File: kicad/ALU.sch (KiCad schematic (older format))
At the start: 41 parts

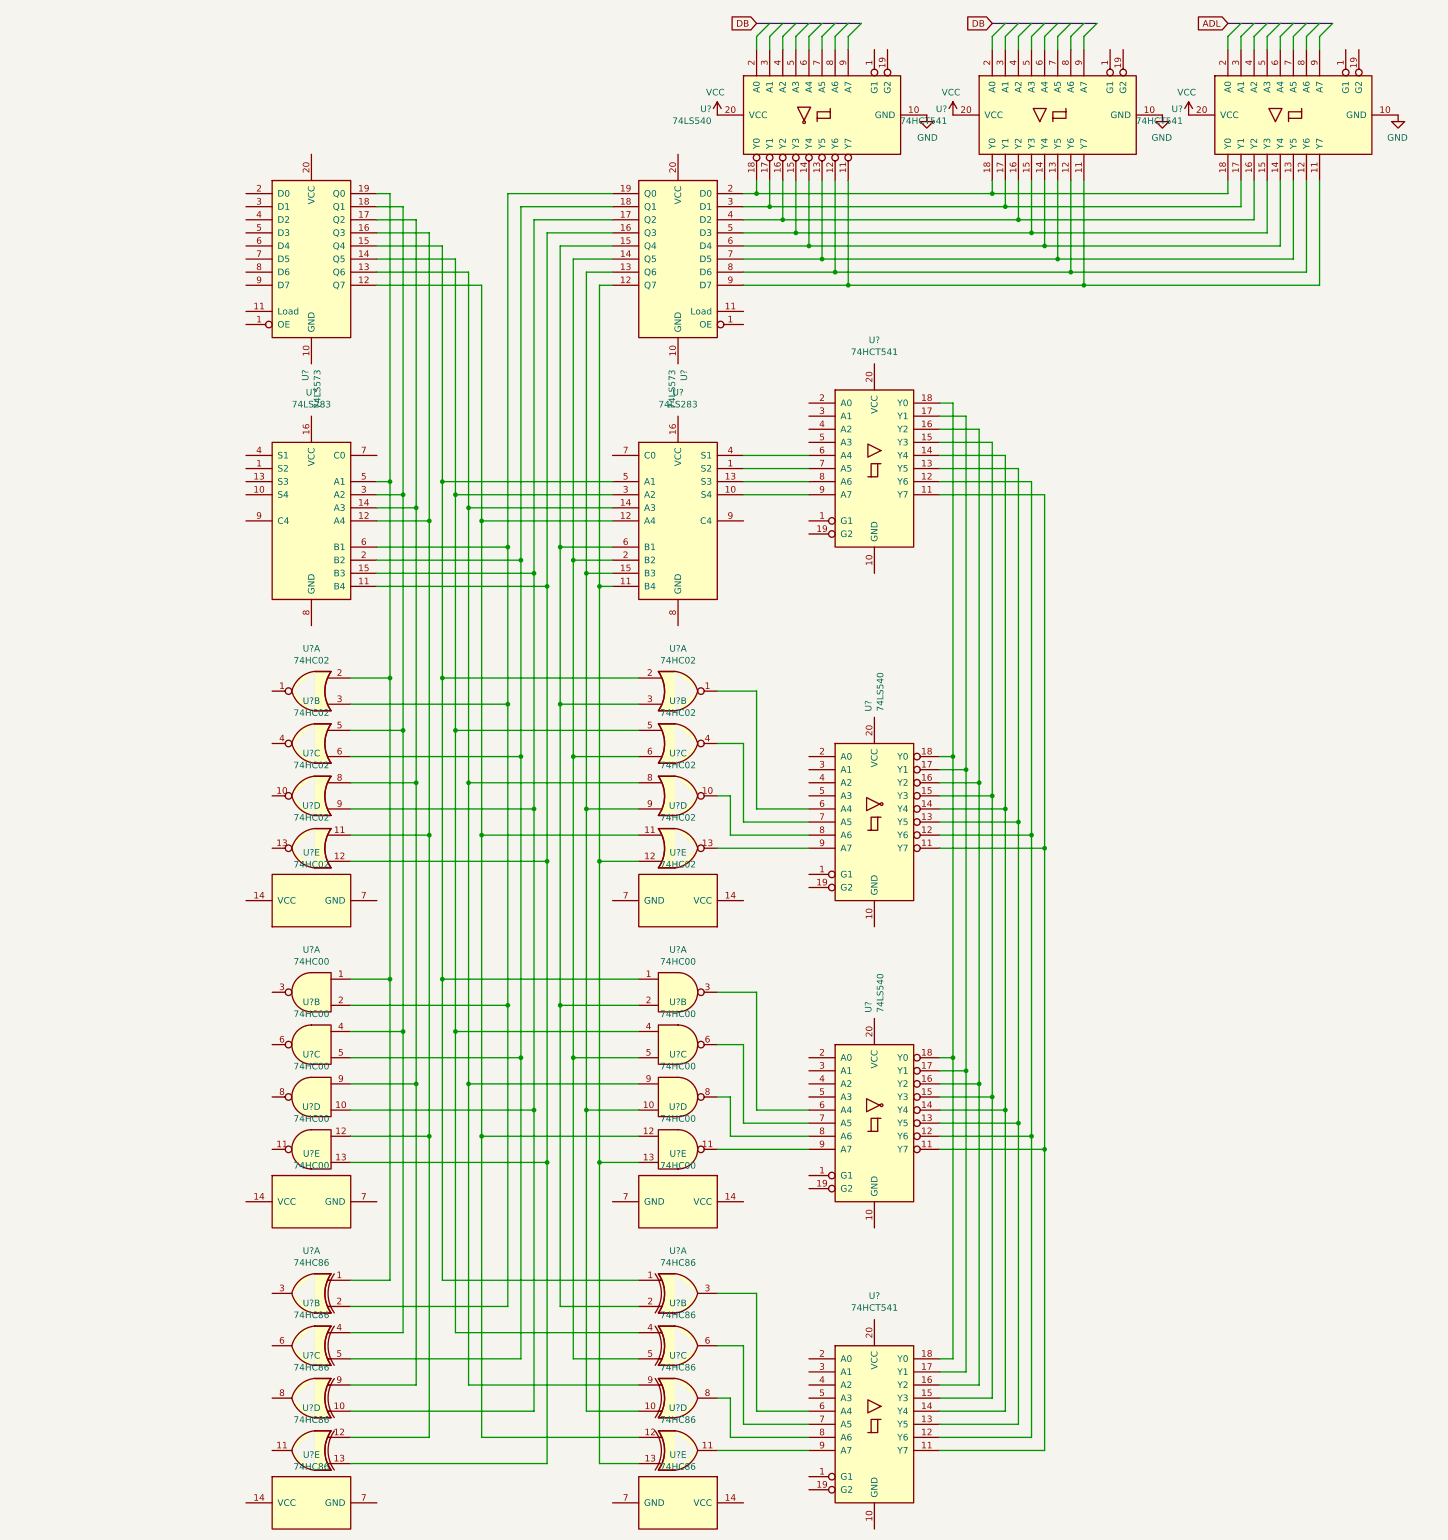
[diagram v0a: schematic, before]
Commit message: add ALU schematic
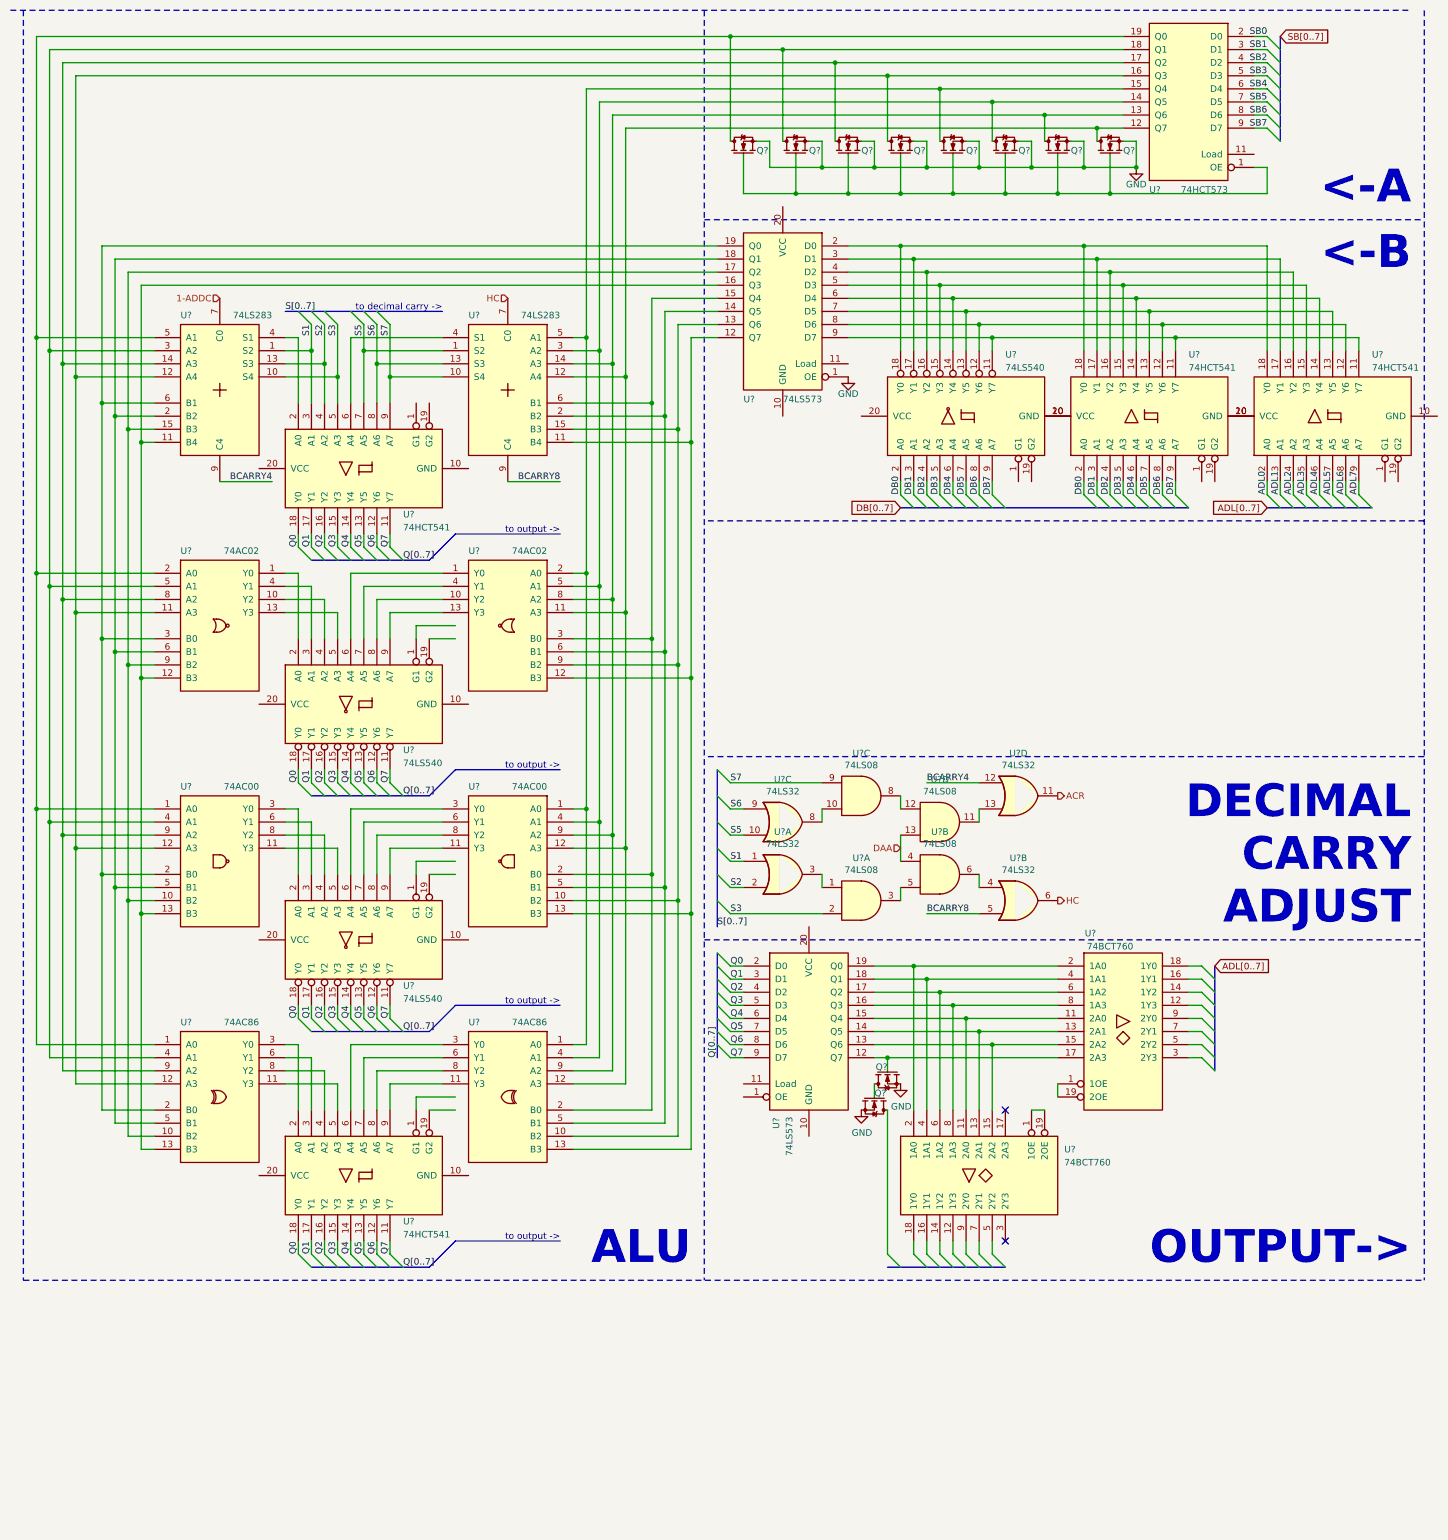
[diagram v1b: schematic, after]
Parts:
- removed U? (x2): 74LS573, symbol 74xx:74LS573
- removed U? (x4): 74HCT541, symbol 74xx:74HCT541
- removed U? (x3): 74LS540, symbol 74xx:74LS540
- removed U? (x2): 74LS283, symbol 74xx:74LS283
- removed U? (x10): 74HC02, symbol 74xx:74HC02
- removed U? (x10): 74HC00, symbol 74xx:74HC00
- removed U? (x10): 74HC86, symbol 74xx:74HC86
- added Q? (x10): VN2106, Package_TO_SOT_THT:TO-92_Inline, symbol 6502:VN2106
- added U? (x2): 74LS573, symbol 74xx:74LS573
- added U? (x3): 74LS540, symbol 74xx:74LS540
- added U?: 74HCT573, symbol 6502:74HCT573
- added U? (x4): 74HCT541, symbol 74xx:74HCT541
- added U? (x2): 74LS283, symbol 6502:74HC283
- added U? (x2): 74BCT760, symbol 6502:74BCT760
- added U? (x2): 74AC02, symbol 6502:74AC02
- added U? (x2): 74AC00, symbol 6502:74AC00
- added U? (x2): 74AC86, symbol 6502:74AC86
- added U? (x4): 74LS32, symbol 74xx:74LS32
- added U? (x4): 74LS08, symbol 74xx:74LS08
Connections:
- net GND: now also Q?.3 (S), Q?.3 (S), Q?.3 (S), Q?.3 (S), Q?.3 (S), Q?.3 (S), Q?.3 (S), Q?.3 (S), Q?.3 (S), Q?.3 (S), U?.1 (OE), U?.10 (GND), U?.10 (GND), U?.10 (GND), U?.7 (GND), U?.7 (GND), U?.7 (GND), U?.7 (GND), U?.7 (GND), U?.7 (GND), U?.8 (GND), U?.8 (GND)
- net VCC: now also U?.14 (VCC), U?.14 (VCC), U?.14 (VCC), U?.14 (VCC), U?.14 (VCC), U?.14 (VCC), U?.16 (VCC), U?.16 (VCC), U?.20 (VCC), U?.20 (VCC), U?.20 (VCC)
- new net: Q?.1 (D), Q?.2 (G)
- new net: Q?.2 (G), U?.12 (Q7), U?.17 (2A3)
- new net: Q?.1 (D), U?.1 (A0), U?.1 (A0), U?.19 (Q0), U?.2 (A0), U?.5 (A1)
- new net: Q?.2 (G), Q?.2 (G), Q?.2 (G), Q?.2 (G), Q?.2 (G), Q?.2 (G), Q?.2 (G), Q?.2 (G), U?.1 (OE)
- new net: Q?.1 (D), U?.18 (Q1), U?.3 (A2), U?.4 (A1), U?.4 (A1), U?.5 (A1)
- new net: Q?.1 (D), U?.14 (A3), U?.17 (Q2), U?.8 (A2), U?.9 (A2), U?.9 (A2)
- new net: Q?.1 (D), U?.11 (A3), U?.12 (A3), U?.12 (A3), U?.12 (A4), U?.16 (Q3)
- new net: Q?.1 (D), U?.1 (A0), U?.1 (A0), U?.15 (Q4), U?.2 (A0), U?.5 (A1)
- new net: Q?.1 (D), U?.14 (Q5), U?.3 (A2), U?.4 (A1), U?.4 (A1), U?.5 (A1)
- new net: Q?.1 (D), U?.13 (Q6), U?.14 (A3), U?.8 (A2), U?.9 (A2), U?.9 (A2)
- new net: Q?.1 (D), U?.11 (A3), U?.12 (A3), U?.12 (A3), U?.12 (A4), U?.12 (Q7)
- new net: U?.11 (B4), U?.12 (B3), U?.12 (Q7), U?.13 (B3), U?.13 (B3)
- new net: U?.10 (B2), U?.10 (B2), U?.13 (Q6), U?.15 (B3), U?.9 (B2)
- new net: U?.14 (Q5), U?.2 (B2), U?.5 (B1), U?.5 (B1), U?.6 (B1)
- new net: U?.15 (Q4), U?.2 (B0), U?.2 (B0), U?.3 (B0), U?.6 (B1)
- new net: U?.11 (B4), U?.12 (B3), U?.13 (B3), U?.13 (B3), U?.16 (Q3)
- new net: U?.10 (B2), U?.10 (B2), U?.15 (B3), U?.17 (Q2), U?.9 (B2)
- new net: U?.18 (Q1), U?.2 (B2), U?.5 (B1), U?.5 (B1), U?.6 (B1)
- new net: U?.19 (Q0), U?.2 (B0), U?.2 (B0), U?.3 (B0), U?.6 (B1)
- new net: U?.18 (Y0), U?.18 (Y0), U?.18 (Y0), U?.2 (D0)
- new net: U?.17 (Y1), U?.17 (Y1), U?.17 (Y1), U?.3 (D1)
- new net: U?.16 (Y2), U?.16 (Y2), U?.16 (Y2), U?.4 (D2)
- new net: U?.15 (Y3), U?.15 (Y3), U?.15 (Y3), U?.5 (D3)
- new net: U?.14 (Y4), U?.14 (Y4), U?.14 (Y4), U?.6 (D4)
- new net: U?.13 (Y5), U?.13 (Y5), U?.13 (Y5), U?.7 (D5)
- new net: U?.12 (Y6), U?.12 (Y6), U?.12 (Y6), U?.8 (D6)
- new net: U?.11 (Y7), U?.11 (Y7), U?.11 (Y7), U?.9 (D7)
- new net: U?.4 (S1), U?.6 (A4)
- new net: U?.2 (A0), U?.4 (S1)
- new net: U?.1 (Y0), U?.2 (A0)
- new net: U?.3 (A1), U?.4 (Y1)
- new net: U?.10 (Y2), U?.4 (A2)
- new net: U?.13 (Y3), U?.5 (A3)
- new net: U?.1 (Y0), U?.6 (A4)
- new net: U?.4 (Y1), U?.7 (A5)
- new net: U?.10 (Y2), U?.8 (A6)
- new net: U?.13 (Y3), U?.9 (A7)
- new net: U?.13 (Q6), U?.15 (2A2), U?.15 (2A2)
- new net: U?.13 (2A1), U?.13 (2A1), U?.14 (Q5)
- new net: U?.11 (2A0), U?.11 (2A0), U?.15 (Q4)
- new net: U?.16 (Q3), U?.8 (1A3), U?.8 (1A3)
- new net: U?.17 (Q2), U?.6 (1A2), U?.6 (1A2)
- new net: U?.18 (Q1), U?.4 (1A1), U?.4 (1A1)
- new net: U?.19 (Q0), U?.2 (1A0), U?.2 (1A0)
- new net: U?.1 (1OE), U?.19 (2OE) (x2)
- new net: U?.2 (A0), U?.3 (Y0) (x2)
- new net: U?.3 (A1), U?.6 (Y1) (x2)
- new net: U?.4 (A2), U?.8 (Y2) (x2)
- new net: U?.11 (Y3), U?.5 (A3) (x2)
- new net: U?.3 (Y0), U?.6 (A4) (x2)
- new net: U?.6 (Y1), U?.7 (A5) (x2)
- new net: U?.8 (A6), U?.8 (Y2) (x2)
- new net: U?.11 (Y3), U?.9 (A7) (x2)
- new net: U?.1, U?.3
- new net: U?.4, U?.6
- new net: U?.10, U?.8
- new net: U?.11, U?.13
- new net: U?.3, U?.5
- new net: U?.12, U?.8
- new net 1-ADDC: U?.7 (C0)
- new net ACR: U?.11
- new net ADL0: U?.2 (A0)
- new net ADL1: U?.3 (A1)
- new net ADL2: U?.4 (A2)
- new net ADL3: U?.5 (A3)
- new net ADL4: U?.6 (A4)
- new net ADL5: U?.7 (A5)
- new net ADL6: U?.8 (A6)
- new net ADL7: U?.9 (A7)
- new net BCARRY4: U?.12, U?.9 (C4)
- new net BCARRY8: U?.5, U?.9 (C4)
- new net DAA: U?.13, U?.4
- new net DB0: U?.2 (A0), U?.2 (A0)
- new net DB1: U?.3 (A1), U?.3 (A1)
- new net DB2: U?.4 (A2), U?.4 (A2)
- new net DB3: U?.5 (A3), U?.5 (A3)
- new net DB4: U?.6 (A4), U?.6 (A4)
- new net DB5: U?.7 (A5), U?.7 (A5)
- new net DB6: U?.8 (A6), U?.8 (A6)
- new net DB7: U?.9 (A7), U?.9 (A7)
- new net HC: U?.6, U?.7 (C0)
- new net Q0: U?.18 (Y0), U?.18 (Y0), U?.18 (Y0), U?.18 (Y0), U?.2 (D0)
- new net Q1: U?.17 (Y1), U?.17 (Y1), U?.17 (Y1), U?.17 (Y1), U?.3 (D1)
- new net Q2: U?.16 (Y2), U?.16 (Y2), U?.16 (Y2), U?.16 (Y2), U?.4 (D2)
- new net Q3: U?.15 (Y3), U?.15 (Y3), U?.15 (Y3), U?.15 (Y3), U?.5 (D3)
- new net Q4: U?.14 (Y4), U?.14 (Y4), U?.14 (Y4), U?.14 (Y4), U?.6 (D4)
- new net Q5: U?.13 (Y5), U?.13 (Y5), U?.13 (Y5), U?.13 (Y5), U?.7 (D5)
- new net Q6: U?.12 (Y6), U?.12 (Y6), U?.12 (Y6), U?.12 (Y6), U?.8 (D6)
- new net Q7: U?.11 (Y7), U?.11 (Y7), U?.11 (Y7), U?.11 (Y7), U?.9 (D7)
- new net S1: U?.1, U?.1 (S2), U?.3 (A1)
- new net S2: U?.13 (S3), U?.2, U?.4 (A2)
- new net S3: U?.10 (S4), U?.2, U?.5 (A3)
- new net S5: U?.1 (S2), U?.10, U?.7 (A5)
- new net S6: U?.13 (S3), U?.8 (A6), U?.9
- new net S7: U?.10 (S4), U?.9, U?.9 (A7)
- new net SB0: U?.2 (D0)
- new net SB1: U?.3 (D1)
- new net SB2: U?.4 (D2)
- new net SB3: U?.5 (D3)
- new net SB4: U?.6 (D4)
- new net SB5: U?.7 (D5)
- new net SB6: U?.8 (D6)
- new net SB7: U?.9 (D7)
- no-connect marks 0 -> 2
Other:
- note added: "<-A"
- note added: "<-B"
- note added: "ALU"
- note added: "DECIMAL\nCARRY\nADJUST"
- note added: "OUTPUT->"
- note added: "to decimal carry ->"
- note added: "to output ->"

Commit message: use custom components
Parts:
- U? (x2): value 74LS573 -> 74HCT573; symbol 74xx:74LS573 -> 6502:74HCT573
- U? (x3): value 74LS540 -> 74HC540; symbol 74xx:74LS540 -> 6502:74HC540
- U? (x4): value 74HCT541 -> 74HC541; symbol 74xx:74HCT541 -> 6502:74HC541
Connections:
- net GND: now also U?.10 (GND), U?.10 (GND), U?.10 (GND), U?.10 (GND), U?.10 (GND), U?.10 (GND), U?.10 (GND), U?.10 (GND), U?.10 (GND)
- net VCC: now also U?.20 (VCC), U?.20 (VCC), U?.20 (VCC), U?.20 (VCC), U?.20 (VCC), U?.20 (VCC), U?.20 (VCC), U?.20 (VCC), U?.20 (VCC)
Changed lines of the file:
@@
 $Descr A3 11693 16535 portrait
 encoding utf-8
-Sheet 3 3
+Sheet 2 2
 Title ""
 Date ""
@@
 	1400 3800 1500 3800
 $Comp
-L 74xx:74HCT541 U?
+L 6502:74HC541 U?
 U 1 1 63074D6C
 P 3100 4000
@@
 AR Path="/628D8D48/63074D6C" Ref="U?"  Part="1"
 F 0 "U?" V 3450 3700 50  0000 R CNN
-F 1 "74HCT541" V 3550 3700 50  0000 R CNN
+F 1 "74HC541" V 3550 3700 50  0000 R CNN
 F 2 "" H 3100 4000 50  0001 C CNN
-F 3 "http://www.ti.com/lit/gpn/sn74HCT541" H 3100 4000 50  0001 C CNN
+F 3 "http://www.ti.com/lit/gpn/sn74LS540" H 3100 4000 50  0001 C CNN
 	1    3100 4000
 	0    -1   1    0
@@
 Q7
 $Comp
-L 74xx:74LS540 U?
+L 6502:74HC540 U?
 U 1 1 63D46498
 P 3100 5800
@@
 AR Path="/628D8D48/63D46498" Ref="U?"  Part="1"
 F 0 "U?" V 3450 5500 50  0000 R CNN
-F 1 "74LS540" V 3550 5500 50  0000 R CNN
+F 1 "74HC540" V 3550 5500 50  0000 R CNN
 F 2 "" H 3100 5800 50  0001 C CNN
 F 3 "http://www.ti.com/lit/gpn/sn74LS540" H 3100 5800 50  0001 C CNN
@@
 $EndComp
 $Comp
-L 74xx:74LS573 U?
+L 6502:74HCT573 U?
 U 1 1 63DA36B1
 P 6500 8300
@@
 AR Path="/628D8D48/63DA36B1" Ref="U?"  Part="1"
 F 0 "U?" V 6250 7600 50  0000 C CNN
-F 1 "74LS573" V 6350 7500 50  0000 C CNN
+F 1 "74HCT573" V 6350 7500 50  0000 C CNN
 F 2 "" H 6500 8300 50  0001 C CNN
 F 3 "74xx/74hc573.pdf" H 6500 8300 50  0001 C CNN
@@
 Q7
 $Comp
-L 74xx:74LS540 U?
+L 6502:74HC540 U?
 U 1 1 65B015A7
 P 3100 7600
@@
 AR Path="/628D8D48/65B015A7" Ref="U?"  Part="1"
 F 0 "U?" V 3450 7300 50  0000 R CNN
-F 1 "74LS540" V 3550 7300 50  0000 R CNN
+F 1 "74HC540" V 3550 7300 50  0000 R CNN
 F 2 "" H 3100 7600 50  0001 C CNN
 F 3 "http://www.ti.com/lit/gpn/sn74LS540" H 3100 7600 50  0001 C CNN
@@
 $EndComp
 $Comp
-L 74xx:74HCT541 U?
+L 6502:74HC541 U?
 U 1 1 66EEAACD
 P 3100 9400
@@
 AR Path="/628D8D48/66EEAACD" Ref="U?"  Part="1"
 F 0 "U?" V 3450 9100 50  0000 R CNN
-F 1 "74HCT541" V 3550 9100 50  0000 R CNN
+F 1 "74HC541" V 3550 9100 50  0000 R CNN
 F 2 "" H 3100 9400 50  0001 C CNN
-F 3 "http://www.ti.com/lit/gpn/sn74HCT541" H 3100 9400 50  0001 C CNN
+F 3 "http://www.ti.com/lit/gpn/sn74LS540" H 3100 9400 50  0001 C CNN
 	1    3100 9400
 	0    -1   1    0
@@
 	5400 2800 5800 2800
 $Comp
-L 74xx:74LS573 U?
+L 6502:74HCT573 U?
 U 1 1 629E37A9
 P 6300 2800
@@
 AR Path="/628D8D48/629E37A9" Ref="U?"  Part="1"
 F 0 "U?" H 6600 2100 50  0000 R BNN
-F 1 "74LS573" H 6000 2100 50  0000 L BNN
+F 1 "74HCT573" H 6000 2100 50  0000 L BNN
 F 2 "" H 6300 2800 50  0001 C CNN
 F 3 "74xx/74hc573.pdf" H 6300 2800 50  0001 C CNN
@@
 $EndComp
 $Comp
-L 74xx:74LS540 U?
+L 6502:74HC540 U?
 U 1 1 629E37AF
 P 7700 3600
@@
 AR Path="/628D8D48/629E37AF" Ref="U?"  Part="1"
 F 0 "U?" V 8200 3300 50  0000 R BNN
-F 1 "74LS540" V 8100 3300 50  0000 R BNN
+F 1 "74HC540" V 8100 3300 50  0000 R BNN
 F 2 "" H 7700 3600 50  0001 C CNN
 F 3 "http://www.ti.com/lit/gpn/sn74LS540" H 7700 3600 50  0001 C CNN
@@
 $EndComp
 $Comp
-L 74xx:74HCT541 U?
+L 6502:74HC541 U?
 U 1 1 629E3A3A
 P 10500 3600
@@
 AR Path="/628D8D48/629E3A3A" Ref="U?"  Part="1"
 F 0 "U?" V 11000 3300 50  0000 R BNN
-F 1 "74HCT541" V 10900 3300 50  0000 R BNN
+F 1 "74HC541" V 10900 3300 50  0000 R BNN
 F 2 "" H 10500 3600 50  0001 C CNN
-F 3 "http://www.ti.com/lit/gpn/sn74HCT541" H 10500 3600 50  0001 C CNN
+F 3 "http://www.ti.com/lit/gpn/sn74LS540" H 10500 3600 50  0001 C CNN
 	1    10500 3600
 	0    -1   -1   0
 $EndComp
 $Comp
-L 74xx:74HCT541 U?
+L 6502:74HC541 U?
 U 1 1 629E3A5D
 P 9100 3600
@@
 AR Path="/628D8D48/629E3A5D" Ref="U?"  Part="1"
 F 0 "U?" V 9600 3300 50  0000 R BNN
-F 1 "74HCT541" V 9500 3300 50  0000 R BNN
+F 1 "74HC541" V 9500 3300 50  0000 R BNN
 F 2 "" H 9100 3600 50  0001 C CNN
-F 3 "http://www.ti.com/lit/gpn/sn74HCT541" H 9100 3600 50  0001 C CNN
+F 3 "http://www.ti.com/lit/gpn/sn74LS540" H 9100 3600 50  0001 C CNN
 	1    9100 3600
 	0    -1   -1   0
@@
 Wire Notes Line width 20
 	500  10200 11200 10200
+Text GLabel 9600 7800 2    50   Input ~ 0
+ADL[0..7]
 Wire Bus Line
 	5800 6300 5800 7500
@@
 Wire Bus Line
 	7200 4300 9400 4300
-Text GLabel 9600 7800 2    50   Input ~ 0
-ADL[0..7]
 $EndSCHEMATC

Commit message: ALU progress
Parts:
- removed Q? (x2): VN2106, Package_TO_SOT_THT:TO-92_Inline, symbol 6502:VN2106
- U? (x2): value 74LS283 -> 74HC283
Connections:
- net ACR: now also U?.11; no longer U?.11
- net ADL0: now also U?.18 (1Y0)
- net ADL1: now also U?.16 (1Y1)
- net ADL2: now also U?.14 (1Y2)
- net ADL3: now also U?.12 (1Y3)
- net ADL4: now also U?.9 (2Y0)
- net ADL5: now also U?.7 (2Y1)
- net ADL6: now also U?.5 (2Y2)
- net ADL7: now also U?.3 (2Y3)
- net BCARRY4: now also U?.9; no longer U?.12
- net BCARRY8: now also U?.13; no longer U?.5
- net DAA: now also U?.2; no longer U?.13
- net HC: now also U?.8; no longer U?.6
- net S1: now also U?.2; no longer U?.1
- net S2: now also U?.1; no longer U?.2
- net S3: now also U?.9; no longer U?.2
- net S5: now also U?.4; no longer U?.10
- net S6: now also U?.5; no longer U?.9
- net S7: now also U?.13; no longer U?.9
- net SB0: now also U?.18 (1Y0)
- net SB1: now also U?.16 (1Y1)
- net SB2: now also U?.14 (1Y2)
- net SB3: now also U?.12 (1Y3)
- net SB4: now also U?.9 (2Y0)
- net SB5: now also U?.7 (2Y1)
- net SB6: now also U?.5 (2Y2)
- net ADD-ADL: now reaches U?.1 (1OE), U?.19 (2OE)
- net ADD-SB06: now reaches U?.1 (1OE), U?.19 (2OE)
- net at U?.6: now also U?.12; no longer U?.4
- net at U?.10: now also U?.3; no longer U?.8
- net at U?.5: now also U?.11; no longer U?.3
- net at U?.8: now also U?.1; no longer U?.12
- new net: U?.12, U?.6
- new net: U?.10, U?.3
- no-connect marks 2 -> 1
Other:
- moved on the sheet: U?, U?B, U?C
